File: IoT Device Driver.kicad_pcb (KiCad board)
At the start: 2 copper layers, 18 parts, among them J1 Conn_01x02, J2 Conn_01x03, J3 Conn_02x04_Odd_Even, J4 Conn_01x02, J5 Screw_Terminal_01x02, J6 Screw_Terminal_01x02, K1 G3MC-202P-VD_DC12, U1 AMS1117-3.3, U2 EL357N-G

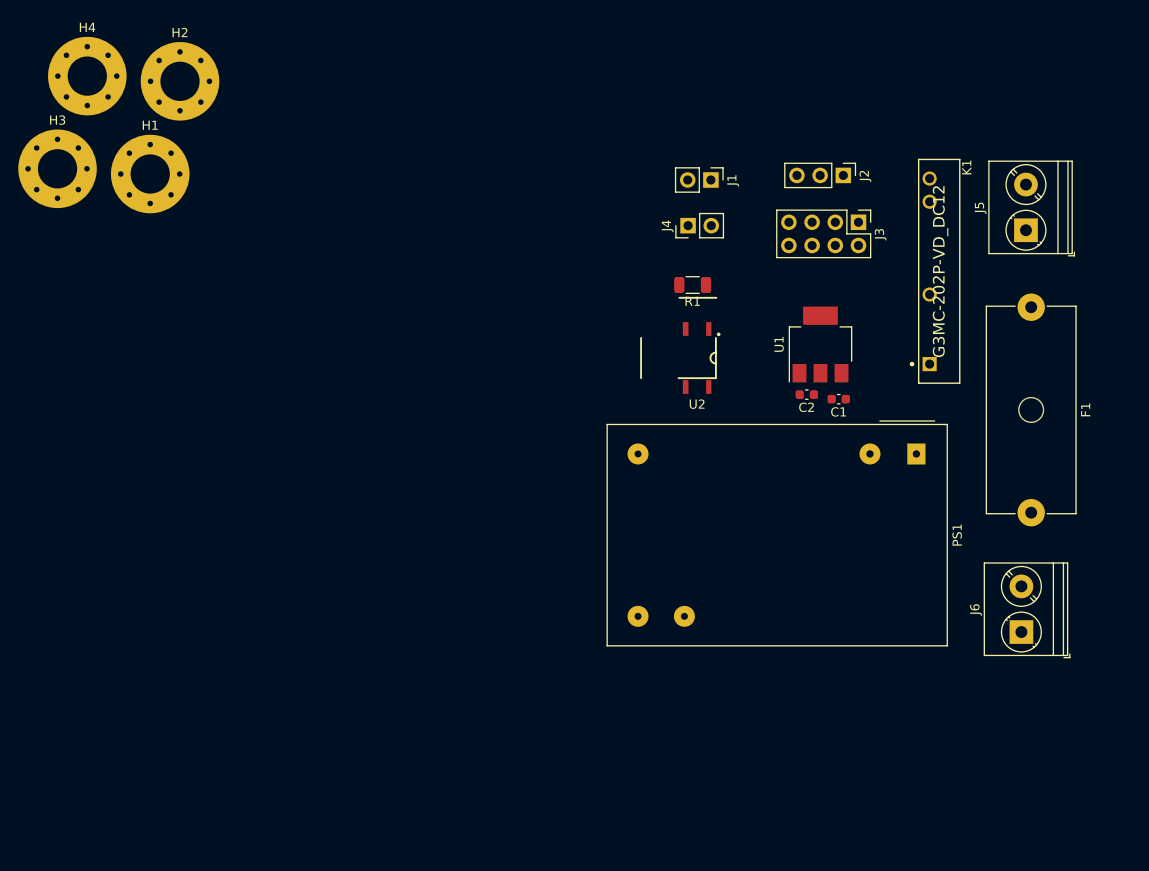
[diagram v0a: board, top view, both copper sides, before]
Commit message: Routing
Routing for low power components over. Things to do: 1)Edit copper fill area, 2(Calculate track width for 3A, 3)Lay track for high power components on bottom layer only
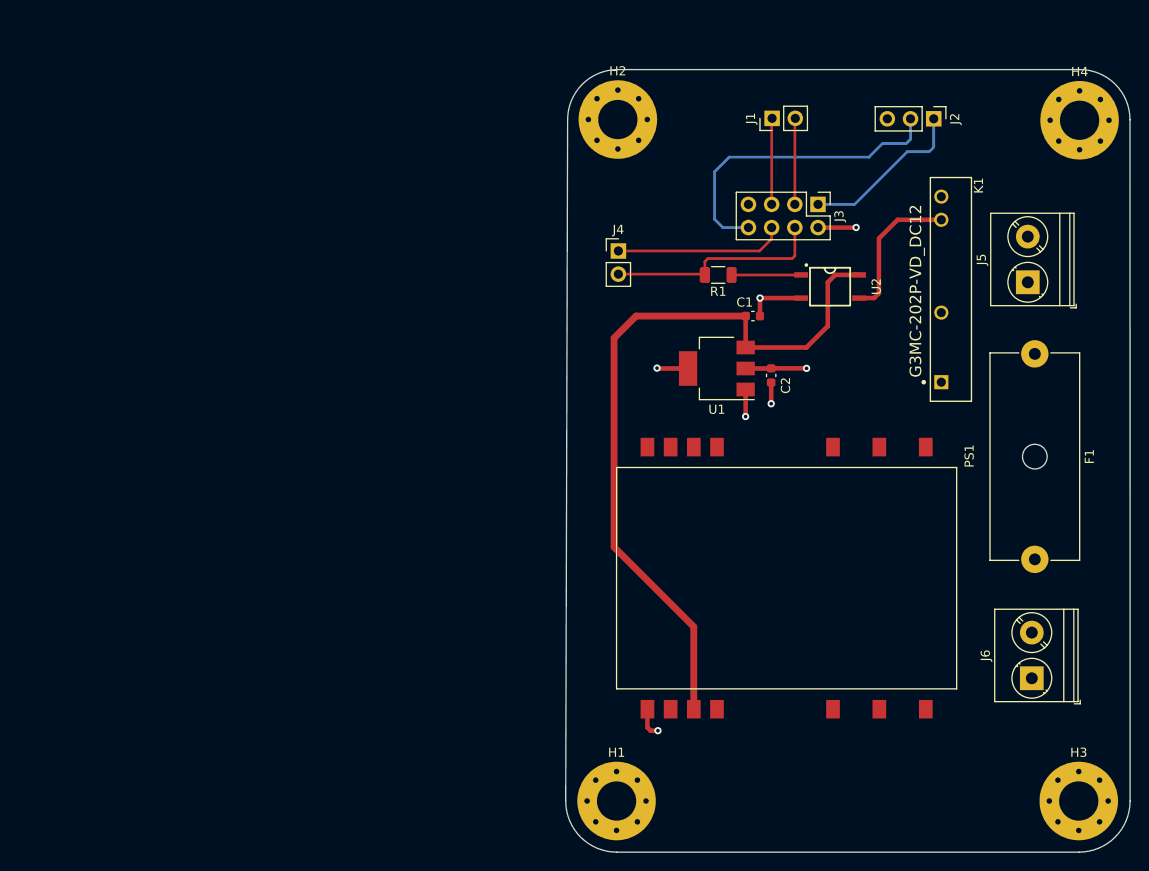
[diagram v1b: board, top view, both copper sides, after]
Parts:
- PS1: footprint Converter_ACDC:Converter_ACDC_MeanWell_IRM-03-xx_THT -> Converter_ACDC:Converter_ACDC_MeanWell_IRM-03-xx_SMD
- moved H3 131.5 mm to (154.8, 161.5)
- moved H4 108.8 mm to (154.9, 87.0)
- moved H1 85.6 mm to (104.2, 161.5)
- moved H2 48.1 mm to (104.3, 86.9)
- moved PS1 19.7 mm to (122.8, 137.1)
- moved U2 16.5 mm to (127.5, 105.2), turned to 270 degrees
- moved C1 13.1 mm to (119.1, 108.4), turned to 0 degrees
- moved J2 11.7 mm to (138.9, 86.8)
- moved U1 11.7 mm to (115.2, 114.1), turned to 180 degrees
- moved J1 9.51 mm to (121.2, 86.8), turned to 90 degrees
- moved J4 8.12 mm to (104.4, 101.3), turned to 0 degrees
- moved J5 5.70 mm to (149.2, 104.7)
- moved J6 5.19 mm to (149.6, 148.1)
- moved F1 5.13 mm to (150.0, 112.5)
- moved J3 4.84 mm to (126.2, 96.2)
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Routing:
- net +5V: track 0.00 -> 82.5 mm
- net Rx: track 0.00 -> 35.2 mm
- net GPIO2: track 0.00 -> 24.2 mm
- net GND: track 0.00 -> 19.2 mm, vias 0 -> 5
- net GPIO0: track 0.00 -> 18.6 mm
- net Tx: track 0.00 -> 18.4 mm
- net Net-(K1-Pad3): track 0.00 -> 16.1 mm
- net +3V3: track 0.00 -> 10.2 mm, vias 0 -> 2
- net RST: track 0.00 -> 9.44 mm
- net CH_EN: track 0.00 -> 9.44 mm
- net Net-(R1-Pad1): track 0.00 -> 7.62 mm
- added copper zone on In2.Cu, net +3V3
- added copper zone on In1.Cu, net GND
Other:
- board outline added: 61.8 x 85.7 mm
- copper layers 2 -> 4

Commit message: PCB Version 1.0 over
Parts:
- added J7: Conn_01x06, Connector_PinSocket_2.54mm:PinSocket_1x06_P2.54mm_Vertical, F.Cu at (118.9, 159.4)
- J1, J4: footprint Connector_PinHeader_2.54mm:PinHeader_1x02_P2.54mm_Vertical -> Connector_PinSocket_2.54mm:PinSocket_1x02_P2.54mm_Vertical
- J2: footprint Connector_PinHeader_2.54mm:PinHeader_1x03_P2.54mm_Vertical -> Connector_PinSocket_2.54mm:PinSocket_1x03_P2.54mm_Vertical
- K1: value G3MC-202P-VD_DC12 -> G3MC-202P-VD_DC5
- moved U1 7.00 mm to (108.2, 112.9)
- moved C2 7.00 mm to (114.2, 113.7)
- moved C1 6.95 mm to (112.2, 107.6)
- moved U2 6.32 mm to (121.3, 106.4)
- moved R1 4.40 mm to (110.9, 103.8)
- moved J5 3.22 mm to (152.4, 105.1)
- moved J6 2.92 mm to (152.4, 147.1)
- moved F1 2.85 mm to (152.8, 112.2)
- moved J3 0.77 mm to (126.2, 95.4)
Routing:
- net NEUT: track 0.00 -> 38.1 mm
- net LINE: track 0.00 -> 29.5 mm
- net +5V: track 82.5 -> 99.5 mm
- net LOAD: track 0.00 -> 16.2 mm
- net GND: track 19.2 -> 7.44 mm
- net Net-(F1-Pad1): track 0.00 -> 7.27 mm
- net Net-(K1-Pad3): track 16.1 -> 19.3 mm
- net +3V3: track 10.2 -> 8.40 mm, vias 2 -> 3
- net Net-(R1-Pad1): track 7.62 -> 6.36 mm
- net GPIO0: track 18.6 -> 19.3 mm
- net RST: track 9.44 -> 8.75 mm
- net CH_EN: track 9.44 -> 8.75 mm
- net Rx: track 35.2 -> 34.8 mm, vias 0 -> 2
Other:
- board text added: "!"
- board text added: "+3V3"
- board text added: "+5V"
- board text added: "230V AC"
- board text added: "CAUTION"
- board text added: "CH_EN"
- board text added: "GND"
- board text added: "GPIO_0"
- board text added: "GPIO_2"
- board text added: "Internet of Things"
- board text added: "IoT Device Contol Printed Circuit Board"
- board text added: "LINE"
- board text added: "LOAD"
- board text added: "NEUTRAL"
- board text added: "RST"
- board text added: "Rx"
- board text added: "Tx"
